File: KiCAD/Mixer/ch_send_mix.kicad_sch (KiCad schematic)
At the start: 1 part, among them U3 NE5532

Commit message: Power Bus, Footprints, Audio Bus
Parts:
- U3: footprint (none) -> Package_SO:SOIC-8_3.9x4.9mm_P1.27mm
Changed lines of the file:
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@@
 			)
 		)
-		(property "Footprint" ""
+		(property "Footprint" "Package_SO:SOIC-8_3.9x4.9mm_P1.27mm"
 			(at 45.72 26.67 0)
 			(hide yes)
@@
 			)
 		)
-		(property "Footprint" ""
+		(property "Footprint" "Package_SO:SOIC-8_3.9x4.9mm_P1.27mm"
 			(at 57.15 66.04 0)
 			(hide yes)
@@
 			)
 		)
-		(property "Footprint" ""
+		(property "Footprint" "Package_SO:SOIC-8_3.9x4.9mm_P1.27mm"
 			(at 57.15 53.34 0)
 			(hide yes)

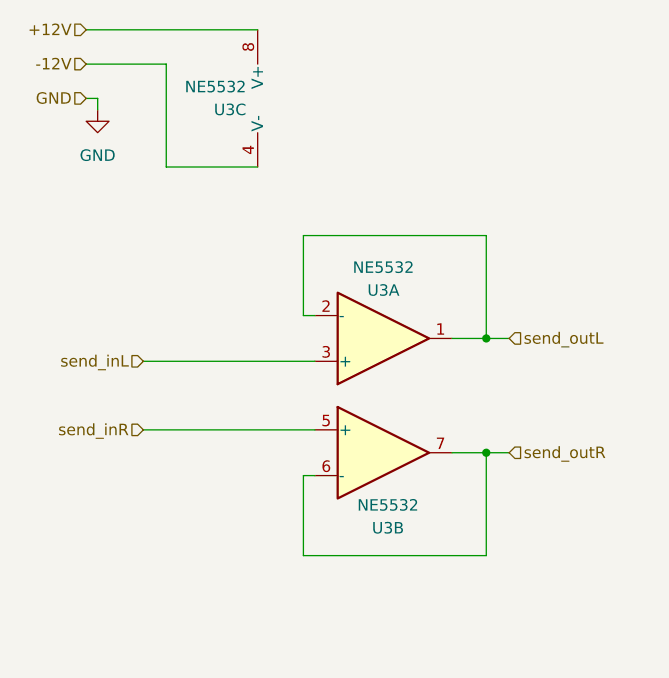
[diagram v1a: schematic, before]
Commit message: added second channel and footprints / created PCB desing...might make PCB bit bigger
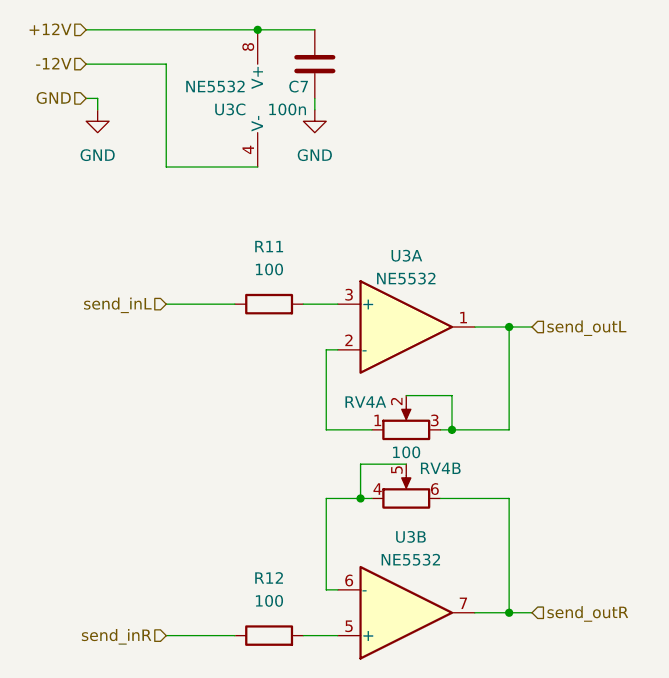
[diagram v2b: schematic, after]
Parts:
- added C7: 100n, Capacitor_SMD:C_0805_2012Metric_Pad1.18x1.45mm_HandSolder, symbol Device:C
- added R11, R12: 100, Resistor_SMD:R_0805_2012Metric_Pad1.20x1.40mm_HandSolder, symbol Device:R
- added RV4: 100, Potentiometer_THT:Potentiometer_Alps_RK09K_Single_Vertical, symbol Device:R_Potentiometer_Dual_Separate
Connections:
- net +12V: now also C7.2
- net GND: now also C7.1
- net send_inL: now also R11.1; no longer U3.3 (+)
- net send_inR: now also R12.1; no longer U3.5 (+)
- net send_outL: now also RV4.2, RV4.3; no longer U3.2 (-)
- net send_outR: now also RV4.6; no longer U3.6 (-)
- new net: R11.2, U3.3 (+)
- new net: RV4.4, RV4.5, U3.6 (-)
- new net: R12.2, U3.5 (+)
- new net: RV4.1, U3.2 (-)
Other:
- moved on the sheet: U3A, U3B

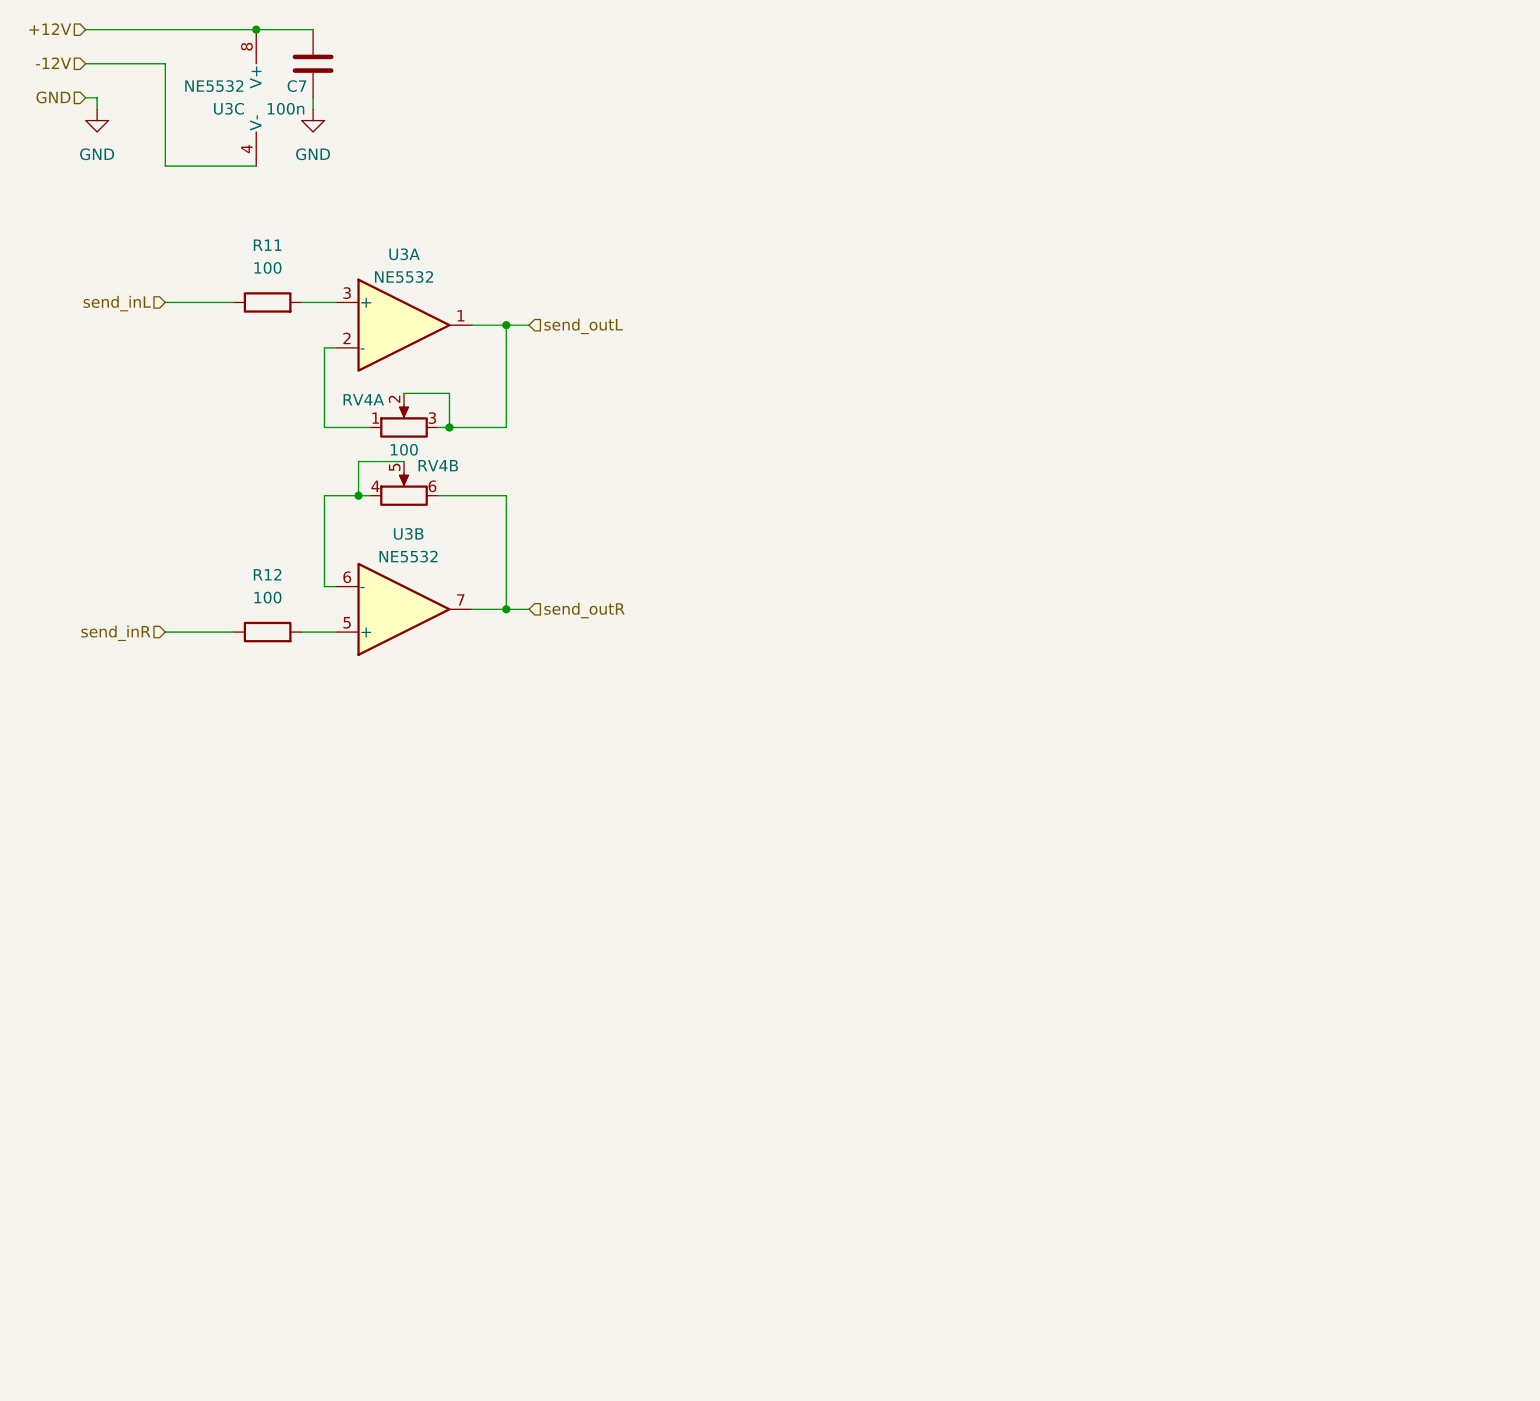
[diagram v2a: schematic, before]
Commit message: Cs an OPV-Strom, Anpassung clicklessmute,...
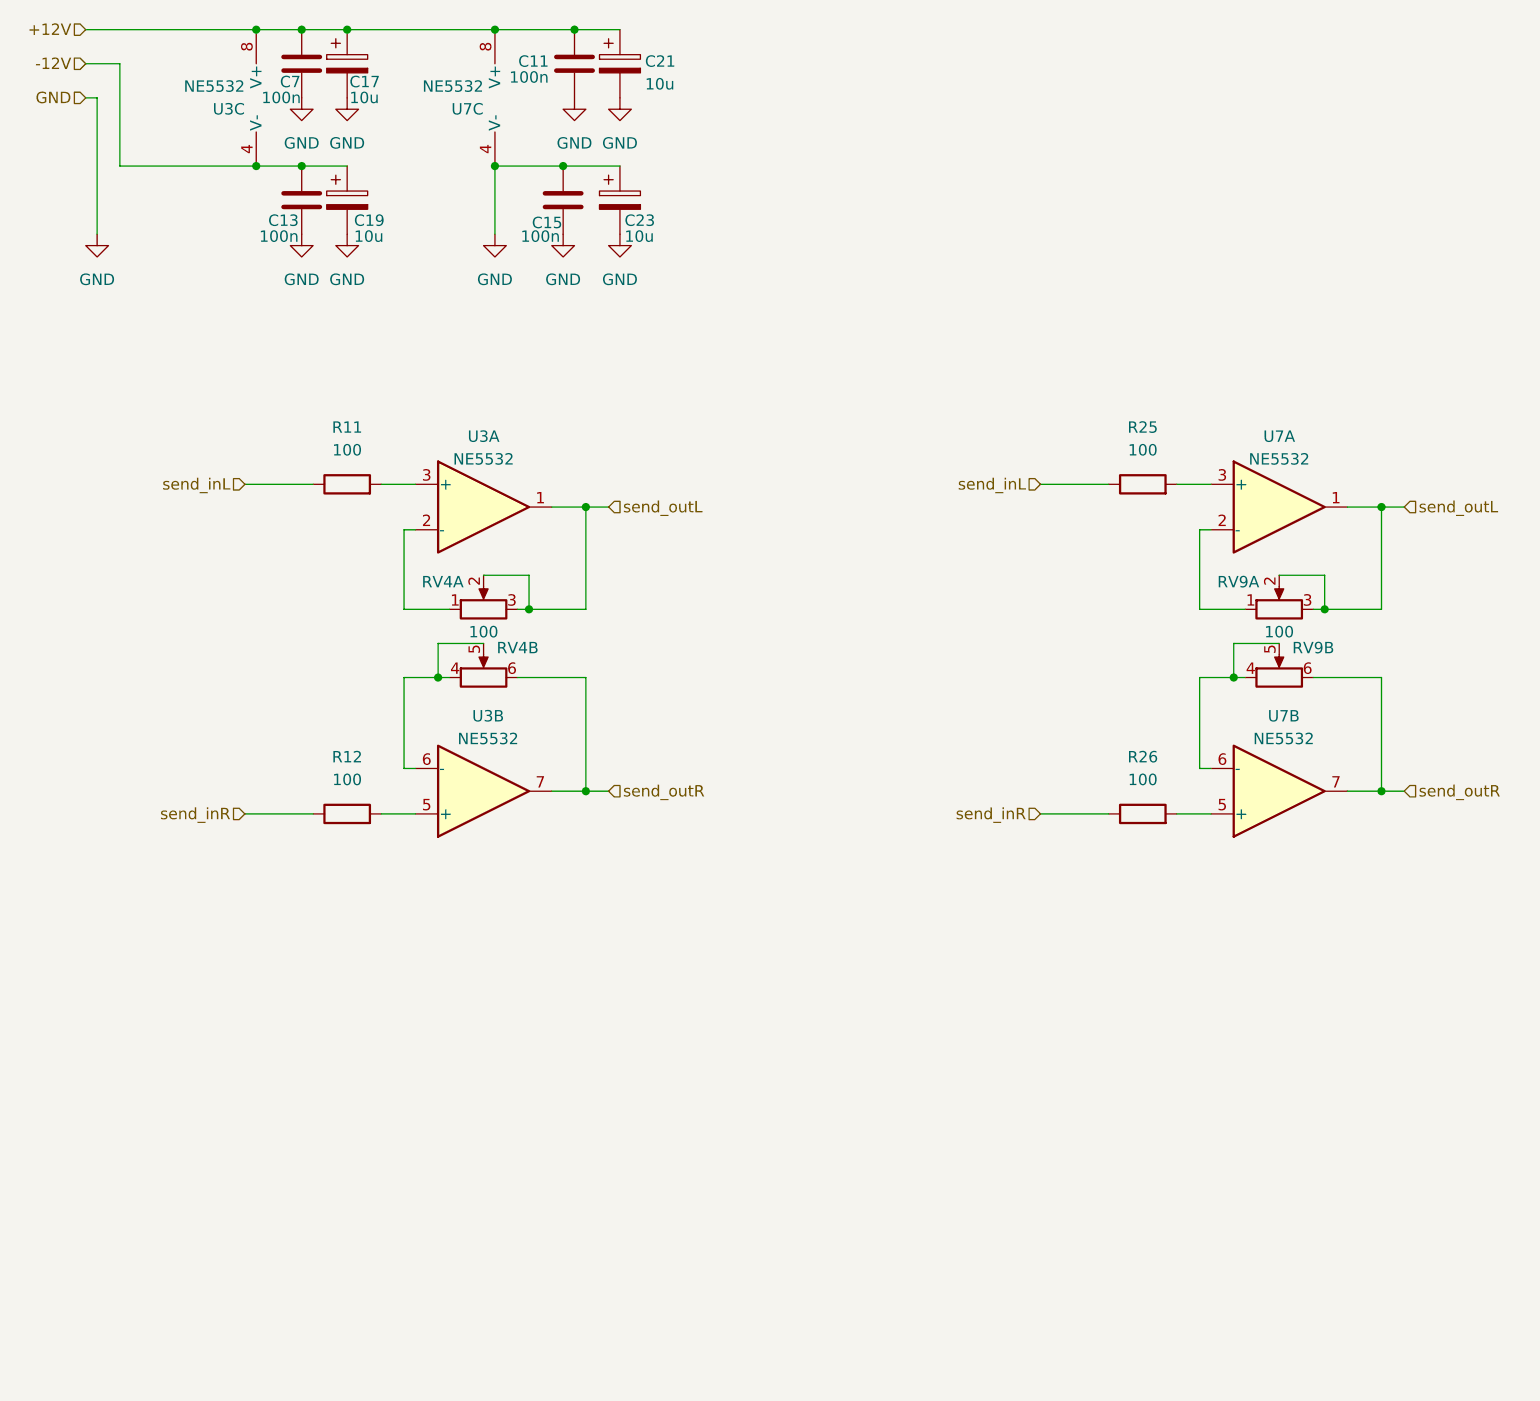
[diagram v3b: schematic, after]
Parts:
- added C11, C13, C15: 100n, Capacitor_SMD:C_0805_2012Metric_Pad1.18x1.45mm_HandSolder, symbol Device:C
- added C17, C19, C21, C23: 10u, Capacitor_SMD:CP_Elec_10x10, symbol Device:C_Polarized
- added R25, R26: 100, Resistor_SMD:R_0805_2012Metric_Pad1.20x1.40mm_HandSolder, symbol Device:R
- added RV9: 100, Potentiometer_THT:Potentiometer_Alps_RK09K_Single_Vertical, symbol Device:R_Potentiometer_Dual_Separate
- added U7: NE5532, Package_SO:SOIC-8_3.9x4.9mm_P1.27mm, symbol Amplifier_Operational:NE5532
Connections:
- net +12V: now also C11.2, C17.1, C21.1, U7.8 (V+)
- net -12V: now also C13.2, C19.1
- net GND: now also C11.1, C13.1, C15.1, C15.2, C17.2, C19.2, C21.2, C23.1, C23.2, U7.4 (V-)
- net send_inL: now also R25.1
- net send_inR: now also R26.1
- net send_outL: now also RV9.2, RV9.3, U7.1
- net send_outR: now also RV9.6, U7.7
- new net: RV9.1, U7.2 (-)
- new net: RV9.4, RV9.5, U7.6 (-)
- new net: R25.2, U7.3 (+)
- new net: R26.2, U7.5 (+)
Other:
- moved on the sheet: C7, R11, R12, RV4A, RV4B, U3A, U3B

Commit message: überarbeitete Schaltung und PCB Desing...v1.0 FERTIG
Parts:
- removed C17, C19, C21, C23: 10u, Capacitor_SMD:CP_Elec_10x10, symbol Device:C_Polarized
- removed R11, R12: 100, Resistor_SMD:R_0805_2012Metric_Pad1.20x1.40mm_HandSolder, symbol Device:R
- removed RV9: 100, Potentiometer_THT:Potentiometer_Alps_RK09K_Single_Vertical, symbol Device:R_Potentiometer_Dual_Separate
- added C12, C14, C16, C8: 100n, Capacitor_SMD:C_0805_2012Metric_Pad1.18x1.45mm_HandSolder, symbol Device:C
- added R23, R24, R39, R40, R43, R44, R45, R46, R47, R48, R49, R50, R51, R52: 1k, Resistor_SMD:R_0805_2012Metric_Pad1.20x1.40mm_HandSolder, symbol Device:R
- added RV10, RV11, RV12: 1k, Potentiometer_THT:Potentiometer_Alps_RK09K_Single_Vertical, symbol Device:R_Potentiometer_Dual_Separate
- added U6, U8: NE5532, Package_SO:SOIC-8_3.9x4.9mm_P1.27mm, symbol Amplifier_Operational:NE5532
- R25, R26, RV4: value 100 -> 1k
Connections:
- net send_inL is gone; now on an unnamed net: R25.1
- net send_inR is gone; now on an unnamed net: R26.1
- net +12V: now also C12.2, C8.2, U6.8 (V+), U8.8 (V+)
- net -12V: now also C15.2, U7.4 (V-), C14.2, C16.2, U6.4 (V-), U8.4 (V-)
- net GND: now also U3.3 (+), U3.5 (+), U7.3 (+), U7.5 (+), C12.1, C14.1, C16.1, C8.1, U6.3 (+), U6.5 (+), U8.3 (+), U8.5 (+); no longer C15.2, U7.4 (V-)
- net at U7.2 (-): now also R44.2, RV11.2, RV11.3, RV12.2, RV12.3
- net at U7.6 (-): now also R40.2, RV11.5, RV11.6, RV12.5, RV12.6
- net at R25.2: now also U7.1, R46.1; no longer U7.3 (+)
- net at RV4.5, U3.6 (-): now also RV4.6, R23.1, R39.2, RV10.5, RV10.6; no longer RV4.4
- net at R26.2: now also U7.7, R45.1; no longer U7.5 (+)
- net at U3.2 (-): now also RV4.2, RV4.3, R24.1, R43.2, RV10.2, RV10.3; no longer RV4.1
- removed net send_outL: RV4.2, RV4.3, U3.1, U7.1
- removed net send_outR: RV4.6, U3.7, U7.7
- new net: R46.2, R47.1, U8.2 (-)
- new net: R23.2, R49.1, U3.7
- new net: R50.2, R51.1, U6.2 (-)
- new net: R45.2, R48.1, U8.6 (-)
- new net: R49.2, R52.1, U6.6 (-)
- new net: R24.2, R50.1, U3.1
- new net pre_send1L: R43.1
- new net pre_send1R: R39.1
- new net pre_send2L: R44.1
- new net pre_send2R: R40.1
- new net send_inL1: RV11.1, RV4.1
- new net send_inL2: RV10.1, RV12.1
- new net send_inR1: RV11.4, RV4.4
- new net send_inR2: RV10.4, RV12.4
- new net send_out1L: R51.2, U6.1
- new net send_out1R: R52.2, U6.7
- new net send_out2L: R47.2, U8.1
- new net send_out2R: R48.2, U8.7
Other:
- note added: "Potidrehung korrekt??"
- moved on the sheet: C11, C15, U7A, U7B, U7C

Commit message: Rework of schematic, with error fixes and reworked pcb
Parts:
- removed C11, C12, C13, C14, C15, C16, C7, C8: 100n, Capacitor_SMD:C_0805_2012Metric_Pad1.18x1.45mm_HandSolder, symbol Device:C
- removed U3, U6, U7: NE5532, Package_SO:SOIC-8_3.9x4.9mm_P1.27mm, symbol Amplifier_Operational:NE5532
- removed unit 3 of U8
- added R35, R36, R37, R38: 0R, Resistor_SMD:R_0805_2012Metric_Pad1.20x1.40mm_HandSolder, symbol Device:R
- added U10, U11, U9: NE5532, Package_SO:SOIC-8_3.9x4.9mm_P1.27mm, symbol Amplifier_Operational:NE5532
- RV5: renamed from RV4; footprint Potentiometer_THT:Potentiometer_Alps_RK09K_Single_Vertical -> Potentiometer_THT:Potentiometer_Alps_RK09L_Double_Vertical
- RV6: renamed from RV10; footprint Potentiometer_THT:Potentiometer_Alps_RK09K_Single_Vertical -> Potentiometer_THT:Potentiometer_Alps_RK09L_Double_Vertical
- RV7: renamed from RV11; footprint Potentiometer_THT:Potentiometer_Alps_RK09K_Single_Vertical -> Potentiometer_THT:Potentiometer_Alps_RK09L_Double_Vertical
- RV8: renamed from RV12; footprint Potentiometer_THT:Potentiometer_Alps_RK09K_Single_Vertical -> Potentiometer_THT:Potentiometer_Alps_RK09L_Double_Vertical
- renumbered R43 to R19, R39 to R20, R44 to R21, R40 to R22, R24 to R23, R23 to R24, R50 to R27, R49 to R28, R46 to R29, R45 to R30, R52 to R31, R51 to R32, R47 to R33, R48 to R34
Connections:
- net GND: now also U10.3 (+), U10.5 (+), U11.3 (+), U11.5 (+), U9.3 (+), U9.5 (+)
- net send_out1L: now also R35.1; no longer R32.2
- net send_out1R: now also R36.1; no longer R31.2
- net send_out2L: now also R37.1; no longer R33.2, U8.1
- net send_out2R: now also R38.1; no longer R34.2, U8.7
- net at R22.2, R26.1, RV7.5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: now also U10.6 (-)
- net at R29.2, R33.1: now also U11.2 (-); no longer U8.2 (-)
- net at R21.2, R25.1, RV7.2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: now also U10.2 (-)
- net at R19.2, R23.1, RV5.2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: now also U8.2 (-)
- net at R26.2, R30.1: now also U10.7
- net at R20.2, R24.1, RV5.5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: now also U8.6 (-)
- net at R25.2, R29.1: now also U10.1
- net at R24.2, R28.1: now also U8.7
- net at R27.2, R32.1: now also U9.2 (-)
- net at R30.2, R34.1: now also U11.6 (-); no longer U8.6 (-)
- net at R28.2, R31.1: now also U9.6 (-)
- net at R23.2, R27.1: now also U8.1
- new net: R33.2, R37.2, U11.1
- new net: R31.2, R36.2, U9.7
- new net: R34.2, R38.2, U11.7
- new net: R32.2, R35.2, U9.1
- no-connect marks 0 -> 2

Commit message: Final PCB Version that got ordered from JLCPCB
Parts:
- R21: renamed from R19; value 1k -> 10k
- R22: renamed from R20; value 1k -> 10k
- R23: renamed from R21; value 1k -> 10k
- R24: renamed from R22; value 1k -> 10k
- R25: renamed from R23; value 1k -> 10k
- R26: renamed from R24; value 1k -> 10k
- R27: renamed from R25; value 1k -> 10k
- R28: renamed from R26; value 1k -> 10k
- RV4: renamed from RV5; value 1k -> 10k
- RV5: renamed from RV6; value 1k -> 10k
- RV6: renamed from RV7; value 1k -> 10k
- RV7: renamed from RV8; value 1k -> 10k
- renumbered R27 to R29, R28 to R30, R29 to R31, R30 to R32, R31 to R33, R32 to R34, R33 to R35, R34 to R36, R35 to R37, R36 to R38, R37 to R39, R38 to R40, U8 to U4, U10 to U5, U9 to U6, U11 to U7
